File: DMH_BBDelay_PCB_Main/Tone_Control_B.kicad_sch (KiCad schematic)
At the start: 9 parts, among them U17 TL072

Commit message: Inverted time and tone control pots
... and added AC coupling to the outputs
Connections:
- net at C50.1, R167.2: now also RV11.4; no longer RV11.6
- net at C49.2, R169.1: now also RV11.6; no longer RV11.4
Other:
- moved on the sheet: RV11B
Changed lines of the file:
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@@
 	(symbol
 		(lib_id "Device:R_Potentiometer_Dual_Separate")
-		(at 76.2 50.8 270)
+		(at 76.2 50.8 90)
+		(mirror x)
 		(unit 2)
 		(body_style 1)
@@
 		(in_pos_files yes)
 		(dnp no)
-		(fields_autoplaced yes)
 		(property "Reference" "RV11"
 			(at 76.2 44.45 90)

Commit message: Scaled up components in Tone Control part
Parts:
- C49, C50: value 33nF -> 3.3nF
- C51: value 22pF -> 33pF
- R166, R168: value 2k2 -> 22k
- R167, R169: value 6k8 -> 68k
- RV11: value B10k -> B100k
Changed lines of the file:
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@@
 			)
 		)
-		(property "Value" "2k2"
+		(property "Value" "22k"
 			(at 101.6 35.052 90)
 			(show_name no)
@@
 			)
 		)
-		(property "Value" "6k8"
+		(property "Value" "68k"
 			(at 57.15 47.752 90)
 			(show_name no)
@@
 			)
 		)
-		(property "Value" "33nF"
+		(property "Value" "3.3nF"
 			(at 76.2 34.036 90)
 			(show_name no)
@@
 			)
 		)
-		(property "Value" "B10k"
+		(property "Value" "B100k"
 			(at 76.2 46.99 90)
 			(show_name no)
@@
 			)
 		)
-		(property "Value" "6k8"
+		(property "Value" "68k"
 			(at 101.6 47.752 90)
 			(show_name no)
@@
 			)
 		)
-		(property "Value" "2k2"
+		(property "Value" "22k"
 			(at 57.15 22.352 90)
 			(show_name no)
@@
 			)
 		)
-		(property "Value" "22pF"
+		(property "Value" "33pF"
 			(at 101.6 59.436 90)
 			(show_name no)
@@
 			)
 		)
-		(property "Value" "33nF"
+		(property "Value" "3.3nF"
 			(at 76.2 21.336 90)
 			(show_name no)

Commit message: Removed compander and adjusted feedback
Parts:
- added C126: 33pF, Capacitor_THT:C_Disc_D3.0mm_W2.0mm_P2.50mm, symbol Device:C
- added R252: 10k, Resistor_THT:R_Axial_DIN0207_L6.3mm_D2.5mm_P7.62mm_Horizontal, symbol Device:R_US
- added R253: 22k, Resistor_THT:R_Axial_DIN0207_L6.3mm_D2.5mm_P7.62mm_Horizontal, symbol Device:R_US
- added U23: TL072, Package_DIP:DIP-8_W7.62mm_Socket, symbol Amplifier_Operational:TL072
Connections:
- net GND: now also R252.1
- net Out: now also C126.2, R253.2, U23.7; no longer C51.2, R168.2, R169.2, U17.7
- new net: C51.2, R168.2, R169.2, U17.7, U23.5 (+)
- new net: C126.1, R252.2, R253.1, U23.6 (-)

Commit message: Synced channel A and B schematics
... and applied several minor improvements and optimizations.
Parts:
- removed U17, U23: TL072, Package_DIP:DIP-8_W7.62mm_Socket, symbol Amplifier_Operational:TL072
- added U17: TL074, Package_DIP:DIP-14_W7.62mm_Socket, symbol Amplifier_Operational:TL074
- R253: value 22k -> 20k
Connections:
- net GND: now also U17.12 (+)
- net Out: now also U17.8
- net at C51.2, R168.2, R169.2: now also U17.10 (+), U17.14
- net at C51.1, RV11.5: now also U17.13 (-)
- net at C126.1, R252.2, R253.1: now also U17.9 (-)
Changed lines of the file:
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@@
-	)
-	(symbol
-		(lib_id "Amplifier_Operational:TL072")
-		(at 101.6 76.2 0)
-		(mirror x)
-		(unit 2)
-		(body_style 1)
-		(exclude_from_sim no)
-		(in_bom yes)
-		(on_board yes)
-		(in_pos_files yes)
-		(dnp no)
-		(property "Reference" "U17"
-			(at 101.6 86.36 0)
-			(show_name no)
-			(do_not_autoplace no)
-			(effects
-				(font
-					(size 1.27 1.27)
-				)
-			)
-		)
-		(property "Value" "TL072"
-			(at 101.6 83.82 0)
-			(show_name no)
-			(do_not_autoplace no)
-			(effects
-				(font
-					(size 1.27 1.27)
-				)
-			)
-		)
-		(property "Footprint" "Package_DIP:DIP-8_W7.62mm_Socket"
-			(at 101.6 76.2 0)
-			(hide yes)
-			(show_name no)
-			(do_not_autoplace no)
-			(effects
-				(font
-					(size 1.27 1.27)
-				)
-			)
-		)
-		(property "Datasheet" "http://www.ti.com/lit/ds/symlink/tl071.pdf"
-			(at 101.6 76.2 0)
-			(hide yes)
-			(show_name no)
-			(do_not_autoplace no)
-			(effects
-				(font
-					(size 1.27 1.27)
-				)
-			)
-		)
-		(property "Description" "Dual Low-Noise JFET-Input Operational Amplifiers, DIP-8/SOIC-8"
-			(at 101.6 76.2 0)
-			(hide yes)
-			(show_name no)
-			(do_not_autoplace no)
-			(effects
-				(font
-					(size 1.27 1.27)
-				)
-			)
-		)
-		(property "Function" ""
-			(at 101.6 76.2 0)
-			(show_name no)
-			(do_not_autoplace no)
-			(effects
-				(font
-					(size 1.27 1.27)
-				)
-			)
-		)
-		(pin "4"
-		)
-		(pin "8"
-		)
-		(pin "1"
-		)
-		(pin "5"
-		)
-		(pin "2"
-		)
-		(pin "3"
-		)
-		(pin "7"
-		)
-		(pin "6"
-		)
-		(instances
-			(project "DMH_BBDelay_PCB_Main"
-				(path "/58f4306d-5387-4983-bb08-41a2313fd315/53120047-129a-4e0f-876f-6cafa2f18733/0b9d8cb9-68a9-4048-b070-e369885a0712"
-					(reference "U17")
-					(unit 2)
-				)
-			)
-		)
 	)
 	(symbol
@@
 	)
 	(symbol
-		(lib_id "Amplifier_Operational:TL072")
+		(lib_id "Amplifier_Operational:TL074")
 		(at 139.7 78.74 0)
-		(unit 2)
-		(body_style 1)
-		(exclude_from_sim no)
-		(in_bom yes)
-		(on_board yes)
-		(in_pos_files yes)
-		(dnp no)
-		(property "Reference" "U23"
+		(unit 3)
+		(body_style 1)
+		(exclude_from_sim no)
+		(in_bom yes)
+		(on_board yes)
+		(in_pos_files yes)
+		(dnp no)
+		(fields_autoplaced yes)
+		(property "Reference" "U17"
 			(at 139.7 68.58 0)
 			(show_name no)
@@
 			)
 		)
-		(property "Value" "TL072"
+		(property "Value" "TL074"
 			(at 139.7 71.12 0)
 			(show_name no)
@@
 			)
 		)
-		(property "Footprint" "Package_DIP:DIP-8_W7.62mm_Socket"
+		(property "Footprint" "Package_DIP:DIP-14_W7.62mm_Socket"
+			(at 138.43 76.2 0)
+			(hide yes)
+			(show_name no)
+			(do_not_autoplace no)
+			(effects
+				(font
+					(size 1.27 1.27)
+				)
+			)
+		)
+		(property "Datasheet" "http://www.ti.com/lit/ds/symlink/tl071.pdf"
+			(at 140.97 73.66 0)
+			(hide yes)
+			(show_name no)
+			(do_not_autoplace no)
+			(effects
+				(font
+					(size 1.27 1.27)
+				)
+			)
+		)
+		(property "Description" "Quad Low-Noise JFET-Input Operational Amplifiers, DIP-14/SOIC-14"
 			(at 139.7 78.74 0)
 			(hide yes)
@@
 			)
 		)
-		(property "Datasheet" "http://www.ti.com/lit/ds/symlink/tl071.pdf"
-			(at 139.7 78.74 0)
-			(hide yes)
-			(show_name no)
-			(do_not_autoplace no)
-			(effects
-				(font
-					(size 1.27 1.27)
-				)
-			)
-		)
-		(property "Description" "Dual Low-Noise JFET-Input Operational Amplifiers, DIP-8/SOIC-8"
-			(at 139.7 78.74 0)
-			(hide yes)
-			(show_name no)
-			(do_not_autoplace no)
-			(effects
-				(font
-					(size 1.27 1.27)
-				)
-			)
-		)
-		(property "Function" ""
-			(at 139.7 78.74 0)
-			(show_name no)
-			(do_not_autoplace no)
-			(effects
-				(font
-					(size 1.27 1.27)
-				)
-			)
+		(pin "1"
+		)
+		(pin "2"
+		)
+		(pin "9"
+		)
+		(pin "3"
+		)
+		(pin "8"
+		)
+		(pin "5"
+		)
+		(pin "7"
+		)
+		(pin "10"
+		)
+		(pin "14"
+		)
+		(pin "6"
 		)
 		(pin "4"
 		)
-		(pin "8"
-		)
-		(pin "1"
-		)
-		(pin "5"
-		)
-		(pin "2"
-		)
-		(pin "3"
-		)
-		(pin "7"
-		)
-		(pin "6"
+		(pin "12"
+		)
+		(pin "13"
+		)
+		(pin "11"
 		)
 		(instances
 			(project "DMH_BBDelay_PCB_Main"
 				(path "/58f4306d-5387-4983-bb08-41a2313fd315/53120047-129a-4e0f-876f-6cafa2f18733/0b9d8cb9-68a9-4048-b070-e369885a0712"
-					(reference "U23")
-					(unit 2)
+					(reference "U17")
+					(unit 3)
+				)
+			)
+		)
+	)
+	(symbol
+		(lib_id "Amplifier_Operational:TL074")
+		(at 101.6 76.2 0)
+		(mirror x)
+		(unit 4)
+		(body_style 1)
+		(exclude_from_sim no)
+		(in_bom yes)
+		(on_board yes)
+		(in_pos_files yes)
+		(dnp no)
+		(property "Reference" "U17"
+			(at 101.6 86.36 0)
+			(show_name no)
+			(do_not_autoplace no)
+			(effects
+				(font
+					(size 1.27 1.27)
+				)
+			)
+		)
+		(property "Value" "TL074"
+			(at 101.6 83.82 0)
+			(show_name no)
+			(do_not_autoplace no)
+			(effects
+				(font
+					(size 1.27 1.27)
+				)
+			)
+		)
+		(property "Footprint" "Package_DIP:DIP-14_W7.62mm_Socket"
+			(at 100.33 78.74 0)
+			(hide yes)
+			(show_name no)
+			(do_not_autoplace no)
+			(effects
+				(font
+					(size 1.27 1.27)
+				)
+			)
+		)
+		(property "Datasheet" "http://www.ti.com/lit/ds/symlink/tl071.pdf"
+			(at 102.87 81.28 0)
+			(hide yes)
+			(show_name no)
+			(do_not_autoplace no)
+			(effects
+				(font
+					(size 1.27 1.27)
+				)
+			)
+		)
+		(property "Description" "Quad Low-Noise JFET-Input Operational Amplifiers, DIP-14/SOIC-14"
+			(at 101.6 76.2 0)
+			(hide yes)
+			(show_name no)
+			(do_not_autoplace no)
+			(effects
+				(font
+					(size 1.27 1.27)
+				)
+			)
+		)
+		(pin "1"
+		)
+		(pin "2"
+		)
+		(pin "9"
+		)
+		(pin "3"
+		)
+		(pin "8"
+		)
+		(pin "5"
+		)
+		(pin "7"
+		)
+		(pin "10"
+		)
+		(pin "14"
+		)
+		(pin "6"
+		)
+		(pin "4"
+		)
+		(pin "12"
+		)
+		(pin "13"
+		)
+		(pin "11"
+		)
+		(instances
+			(project "DMH_BBDelay_PCB_Main"
+				(path "/58f4306d-5387-4983-bb08-41a2313fd315/53120047-129a-4e0f-876f-6cafa2f18733/0b9d8cb9-68a9-4048-b070-e369885a0712"
+					(reference "U17")
+					(unit 4)
 				)
 			)
@@
 			)
 		)
-		(property "Value" "22k"
+		(property "Value" "20k"
 			(at 139.7 104.648 90)
 			(show_name no)

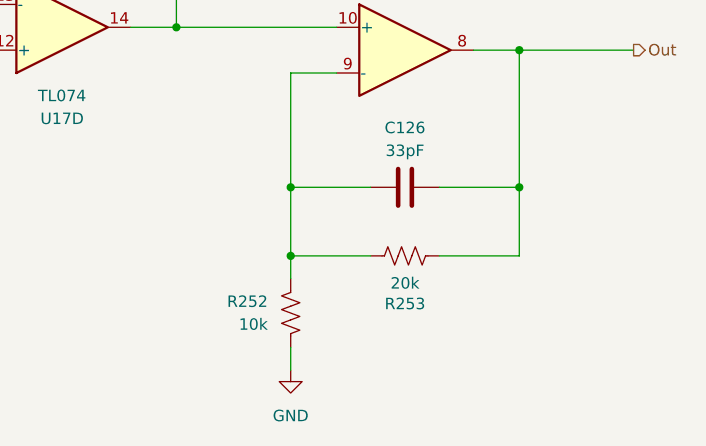
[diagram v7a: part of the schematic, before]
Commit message: Validated gains in breadboard
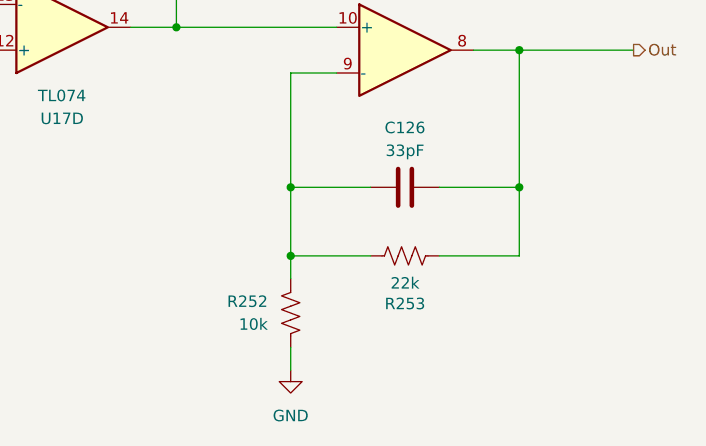
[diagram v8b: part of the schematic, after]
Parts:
- R253: value 20k -> 22k
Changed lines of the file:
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@@
 			)
 		)
-		(property "Value" "20k"
+		(property "Value" "22k"
 			(at 139.7 104.648 90)
 			(show_name no)
